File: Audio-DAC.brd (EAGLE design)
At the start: 99 x 99 mm, 211 parts, among them CON1 USB-5075BR-04-WH, CON2 VOL_CON, CON3 SWD_CON, IC1 3.3V 200mA, IC10 15V, IC11 -15V, IC12 3.3V, IC13 LPC1114FDH28, IC14 7812, IC15 5V, IC16 5V, IC17 3.3V, IC18 TC7WH74FU, IC19 AK4495EQ, IC2 AT32UC3A3256, IC20 TC7WU04FU, IC21 9V, IC22 -9V, IC23 OP275, IC3 OCT_BUFFER-SO6, IC4 OCT_BUFFER-SO6, IC5 OCT_BUFFER-SO6, IC6 OCT_BUFFER-SO6, IC7 OCT_BUFFER-SO6, IC8 OCT_BUFFER-SO6, IC9 7805, Q1 NPN2SC3422, Q2 PNP2SA1359, Q3 NPN2SC3422, Q4 PNP2SA1359, Q5 NPN2SC3325, Q6 NPN2SC3325, SW1 EA2, SW2 EA2, X1 12MHz, X2 22.5792MHz, X3 24.576MHz

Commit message: 微修正
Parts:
- added FB3: FB-1608, my_rcl:1608
- IC14: value 7812 -> 10V; device my_ic:TO-220 -> my_ic:REGULATOR_LED
- IC21: value 9V -> 10V
- IC22: value -9V -> -10V
- moved IC14 2.54 mm to (38.7, 53.3), turned to 0 degrees
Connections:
- new net N$56: C26.1, FB3.2, IC9.1
- net +12V: now also FB3.1, IC14.1; no longer C26.1, IC14.3, IC9.1
- net V+: now also IC14.3; no longer IC14.1
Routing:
- net N$56: track 0.00 -> 3.52 mm
- net V+: track 150.7 -> 148.1 mm
- net +12V: track 90.6 -> 88.7 mm
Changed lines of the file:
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@@
 <attribute name="VALUE" x="32.004" y="41.656" size="0.8128" layer="27"/>
 </element>
-<element name="IC14" library="my_ic" package="TO-220" value="7812" x="36.195" y="53.34" smashed="yes" rot="R180">
-<attribute name="NAME" x="42.8625" y="53.6575" size="0.8128" layer="25" rot="R180"/>
-<attribute name="VALUE" x="40.9575" y="55.88" size="0.8128" layer="27" rot="R180"/>
+<element name="IC14" library="my_ic" package="REGULATOR_LED" value="10V" x="38.735" y="53.34" smashed="yes">
+<attribute name="NAME" x="32.0675" y="53.0225" size="0.8128" layer="25"/>
+<attribute name="VALUE" x="33.9725" y="50.8" size="0.8128" layer="27"/>
 </element>
 <element name="IC15" library="my_ic" package="REGULATOR_LED" value="5V" x="27.94" y="77.47" smashed="yes">
@@
 <attribute name="VALUE" x="20.0025" y="18.415" size="0.8128" layer="28" rot="MR270"/>
 </element>
-<element name="IC21" library="my_ic" package="REGULATOR_LED" value="9V" x="43.18" y="62.23" smashed="yes">
+<element name="IC21" library="my_ic" package="REGULATOR_LED" value="10V" x="43.18" y="62.23" smashed="yes">
 <attribute name="NAME" x="36.195" y="64.135" size="0.8128" layer="25"/>
 <attribute name="VALUE" x="45.72" y="58.42" size="0.8128" layer="27"/>
 </element>
-<element name="IC22" library="my_ic" package="REGULATOR_LED" value="-9V" x="43.18" y="58.42" smashed="yes" rot="R180">
+<element name="IC22" library="my_ic" package="REGULATOR_LED" value="-10V" x="43.18" y="58.42" smashed="yes" rot="R180">
 <attribute name="NAME" x="48.895" y="55.88" size="0.8128" layer="25" rot="R180"/>
 <attribute name="VALUE" x="40.64" y="62.23" size="0.8128" layer="27" rot="R180"/>
@@
 <attribute name="NAME" x="28.905" y="40.75125" size="0.8128" layer="25" rot="R180"/>
 <attribute name="VALUE" x="28.905" y="41.01125" size="0.8128" layer="27" rot="R180"/>
+</element>
+<element name="FB3" library="my_rcl" package="1608" value="FB-1608" x="29.5275" y="48.895" smashed="yes" rot="MR270">
+<attribute name="NAME" x="28.5275" y="50.495" size="0.8128" layer="26" rot="MR270"/>
+<attribute name="VALUE" x="31.3275" y="50.495" size="0.8128" layer="28" rot="MR270"/>
 </element>
 </elements>
@@
 <contactref element="IC10" pad="1"/>
 <contactref element="C35" pad="+"/>
-<contactref element="IC14" pad="1"/>
+<contactref element="IC14" pad="3"/>
 <contactref element="IC21" pad="3"/>
 <contactref element="Q1" pad="2"/>
@@
 <wire x1="58.42" y1="71.755" x2="58.42" y2="64.77" width="1.27" layer="16"/>
 <wire x1="54.61" y1="62.23" x2="45.72" y2="62.23" width="1.27" layer="1"/>
-<wire x1="38.735" y1="53.34" x2="49.53" y2="53.34" width="1.27" layer="1"/>
+<wire x1="41.275" y1="53.34" x2="49.53" y2="53.34" width="1.27" layer="1"/>
 <wire x1="49.53" y1="53.34" x2="52.705" y2="53.34" width="1.27" layer="1"/>
 <wire x1="49.53" y1="53.34" x2="49.53" y2="46.99" width="1.27" layer="1"/>
@@
 <signal name="+12V">
 <contactref element="IC15" pad="3"/>
-<contactref element="IC14" pad="3"/>
+<contactref element="IC14" pad="1"/>
 <contactref element="C39" pad="+"/>
 <contactref element="IC16" pad="3"/>
@@
 <contactref element="SW2" pad="10"/>
 <contactref element="TP20" pad="1"/>
-<contactref element="IC9" pad="1"/>
-<contactref element="C26" pad="1"/>
-<wire x1="27.8875" y1="47.9425" x2="27.8875" y2="50.7475" width="0.6096" layer="16"/>
 <wire x1="27.8875" y1="50.7475" x2="27.94" y2="50.8" width="0.6096" layer="16"/>
-<wire x1="27.8875" y1="47.9425" x2="27.8875" y2="46.46125" width="0.6096" layer="16"/>
-<wire x1="27.8875" y1="46.46125" x2="27.6225" y2="46.19625" width="0.6096" layer="16"/>
 <wire x1="30.48" y1="81.28" x2="30.48" y2="77.47" width="1.905" layer="16"/>
 <wire x1="30.48" y1="77.47" x2="30.48" y2="75.8825" width="1.905" layer="16"/>
@@
 <wire x1="29.21" y1="54.2925" x2="27.94" y2="53.0225" width="1.905" layer="16"/>
 <wire x1="27.94" y1="53.0225" x2="27.94" y2="50.8" width="1.905" layer="16"/>
-<wire x1="27.94" y1="50.8" x2="32.385" y2="50.8" width="1.905" layer="16"/>
-<wire x1="32.385" y1="50.8" x2="33.655" y2="52.07" width="1.905" layer="16"/>
-<wire x1="33.655" y1="52.07" x2="33.655" y2="53.34" width="1.905" layer="16"/>
+<wire x1="27.94" y1="50.8" x2="29.5275" y2="50.8" width="1.905" layer="16"/>
+<wire x1="29.5275" y1="50.8" x2="32.385" y2="50.8" width="1.905" layer="16"/>
+<wire x1="32.385" y1="50.8" x2="34.925" y2="53.34" width="1.905" layer="16"/>
+<wire x1="34.925" y1="53.34" x2="36.195" y2="53.34" width="1.905" layer="16"/>
 <wire x1="85.09" y1="71.12" x2="85.09" y2="73.025" width="0.3048" layer="1"/>
 <wire x1="87.9475" y1="75.8825" x2="87.9475" y2="80.63" width="0.3048" layer="1"/>
@@
 <wire x1="88.5825" y1="93.6625" x2="88.5825" y2="89.2175" width="0.6096" layer="16"/>
 <wire x1="90.805" y1="86.995" x2="88.5825" y2="89.2175" width="0.6096" layer="16"/>
-<wire x1="33.02" y1="64.4525" x2="85.09" y2="71.12" width="0" layer="19" extent="1-1"/>
+<contactref element="FB3" pad="1"/>
+<wire x1="29.5275" y1="49.795" x2="29.5275" y2="50.8" width="0.8128" layer="16"/>
+<wire x1="36.195" y1="53.34" x2="85.09" y2="71.12" width="0" layer="19" extent="1-1"/>
 </signal>
 <signal name="N$83">
@@
 <wire x1="29.86375" y1="39.21125" x2="30.065" y2="39.01" width="0.3048" layer="1"/>
 </signal>
+<signal name="N$56">
+<contactref element="IC9" pad="1"/>
+<contactref element="C26" pad="1"/>
+<wire x1="27.8875" y1="47.9425" x2="27.8875" y2="46.46125" width="0.6096" layer="16"/>
+<wire x1="27.8875" y1="46.46125" x2="27.6225" y2="46.19625" width="0.6096" layer="16"/>
+<contactref element="FB3" pad="2"/>
+<wire x1="29.5275" y1="47.995" x2="29.475" y2="47.9425" width="0.8128" layer="16"/>
+<wire x1="29.475" y1="47.9425" x2="27.8875" y2="47.9425" width="0.8128" layer="16"/>
+</signal>
 </signals>

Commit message: ビアを打った
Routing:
- net VBUS: track 14.6 -> 15.1 mm
- net DGND: track 70.0 -> 70.4 mm, vias 27 -> 120
- added copper zone on layer 1, net DGND
- added copper zone on layer 16, net DGND
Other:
- board text added: "Audio DAC v6"
- board text removed: "Audio DAC ver6"

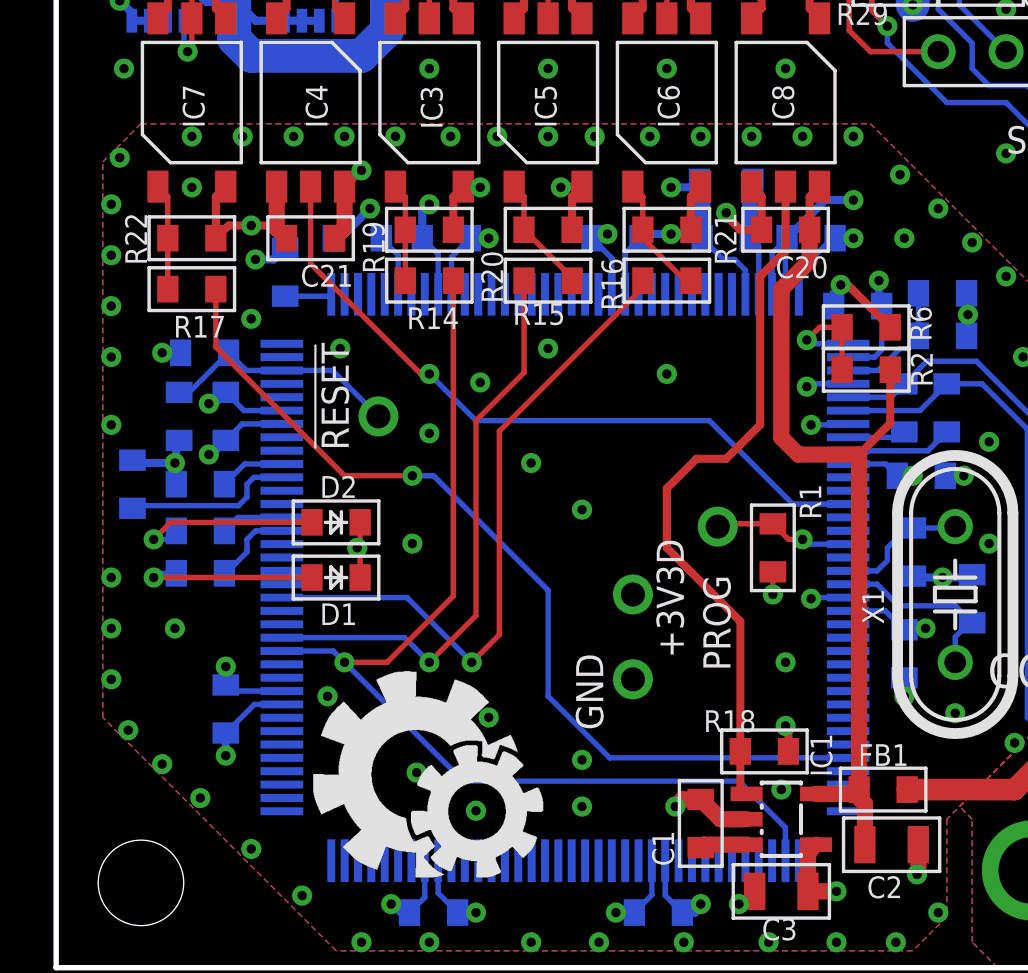
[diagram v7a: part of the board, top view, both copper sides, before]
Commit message: フォトカプラを反転
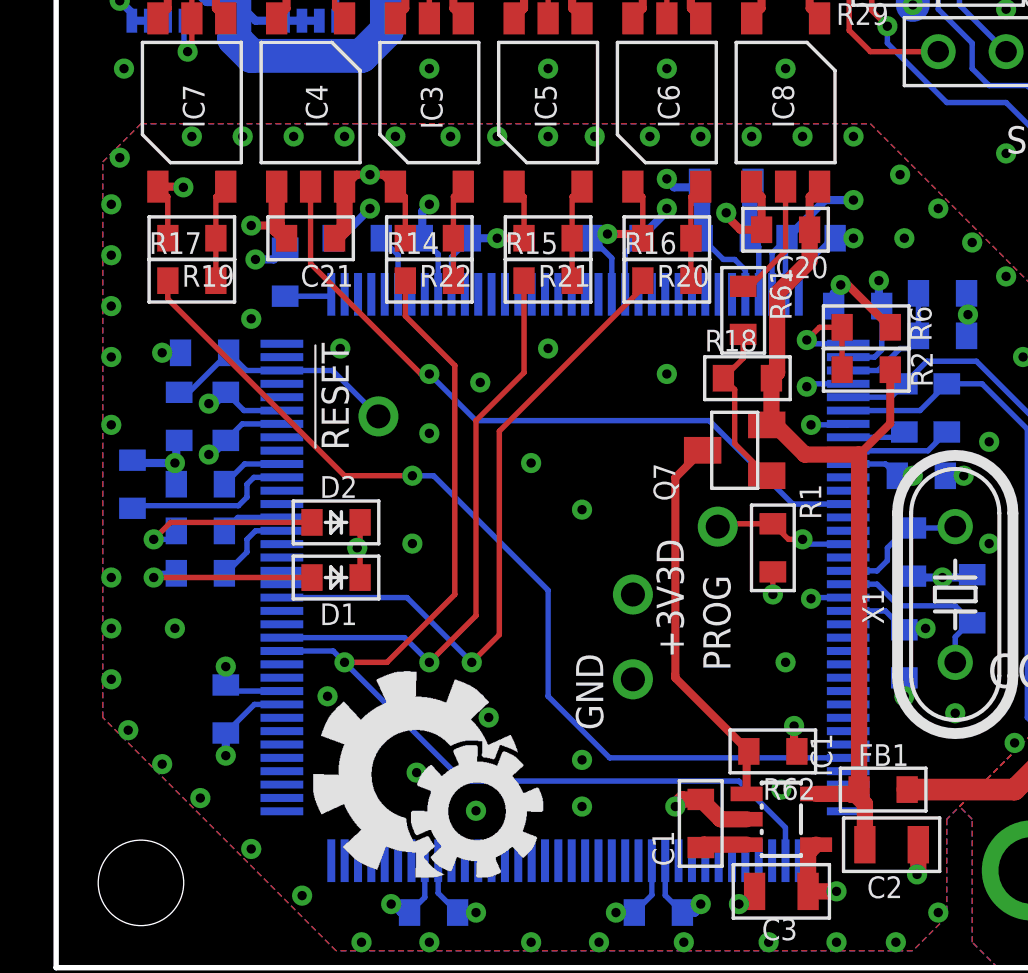
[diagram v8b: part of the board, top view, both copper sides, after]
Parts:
- added Q7: PNP2SA1313, my_ic:SC59
- added R61, R62: 1.5k, my_rcl:1608
- R18: value 10k -> 1.5k
- moved R18 14.0 mm to (25.9, 22.1), turned to 0 degrees
- moved R19 8.90 mm to (5.08, 27.3)
- moved R22 8.89 mm to (14.0, 27.3)
- moved R20 4.46 mm to (22.9, 27.3)
- moved R21 4.46 mm to (18.4, 27.3)
- moved R17 0.32 mm to (5.08, 25.7), turned to 0 degrees
- turned R14 to 0 degrees
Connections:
- new net N$58: IC6.3, R16.2, R20.1
- new net N$61: IC7.3, R17.2, R19.1
- net +3V3D: now also IC4.1, IC5.1, IC6.1, IC7.1, R19.2, R20.2, R21.2, R22.2
- net DGND: now also R62.1; no longer IC4.3, IC5.3, IC6.3, IC7.3, R18.1, R19.1, R20.1, R21.1, R22.1
- net EN_+3V3D: now also Q7.3, R62.2; no longer IC8.5, R18.2
- net N$14: now also Q7.1, R18.1, R61.2; no longer IC7.1, R17.2, R22.2
- net N$15: now also IC4.3, R22.1; no longer IC4.1, R19.2
- net N$16: now also IC8.5, R61.1; no longer IC5.1, R15.2, R20.2
- net N$17: now also IC5.3, R15.2, R21.1; no longer IC6.1, R16.2, R21.2
- net USB_VBUS: now also Q7.2, R18.2
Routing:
- net +3V3D: track 47.2 -> 60.6 mm, vias 15 -> 16
- net EN_+3V3D: track 26.5 -> 14.5 mm
- net DGND: track 70.4 -> 59.8 mm, vias 120 -> 117
- net N$61: track 0.00 -> 3.67 mm
- net N$58: track 0.00 -> 3.67 mm
- net N$14: track 3.99 -> 6.27 mm
- net D_EN_48K: track 34.5 -> 35.6 mm
- net N$17: track 4.54 -> 3.67 mm
- net D_SCK: track 39.7 -> 40.5 mm
